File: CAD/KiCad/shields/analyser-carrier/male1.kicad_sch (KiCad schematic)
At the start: 5 parts, among them M4 DFRobot DFR0126 Audio Analyze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

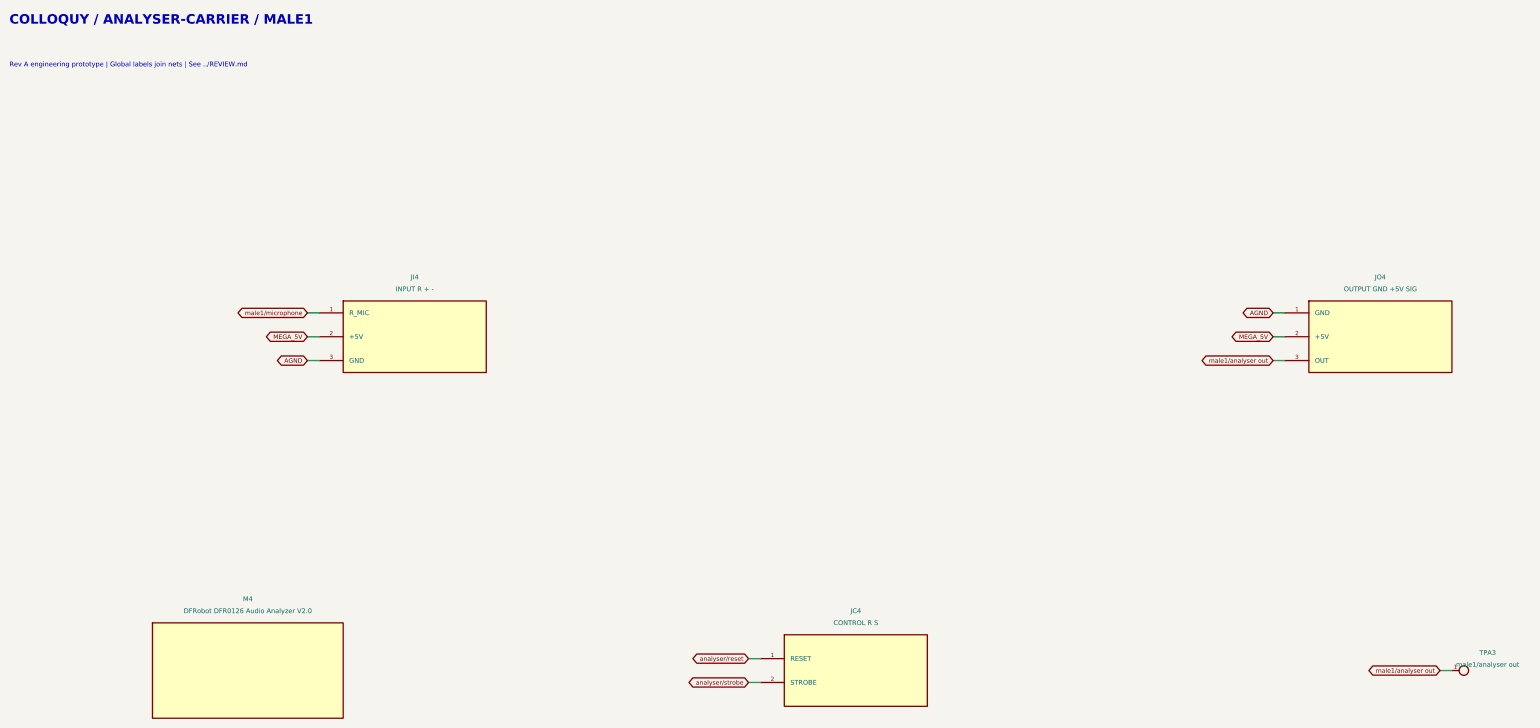
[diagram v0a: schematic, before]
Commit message: Convert analyser carrier to direct sockets for modified DFRobot modules
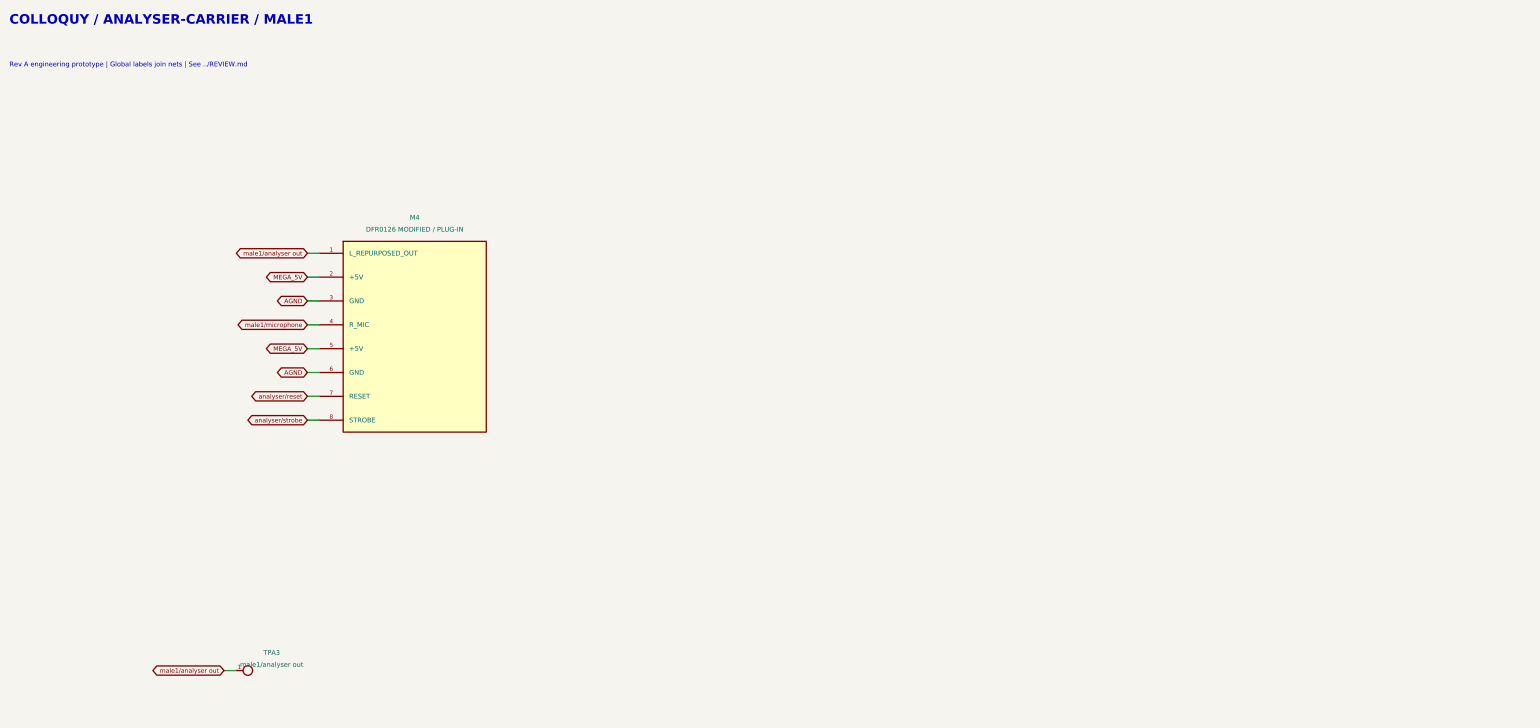
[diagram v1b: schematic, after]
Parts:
- removed JC4: CONTROL R S, Shields:PinHeader_1x02_P2.54mm_Vertical, symbol Colloquy:JC4
- removed JI4: INPUT R + -, Shields:PinHeader_1x03_P2.54mm_Vertical, symbol Colloquy:JI4
- removed JO4: OUTPUT GND +5V SIG, Shields:PinHeader_1x03_P2.54mm_Vertical, symbol Colloquy:JO4
- M4: value DFRobot DFR0126 Audio Analyzer V2.0 -> DFR0126 MODIFIED / PLUG-IN; footprint Shields:DFR0126_PhotoMount -> Shields:DFR0126_PlugIn_Photo
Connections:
- net AGND: now also M4.3 (GND), M4.6 (GND)
- net MEGA_5V: now also M4.2 (+5V), M4.5 (+5V)
- net analyser/reset: now also M4.7 (RESET)
- net analyser/strobe: now also M4.8 (STROBE)
- net male1/analyser out: now also M4.1 (L_REPURPOSED_OUT)
- net male1/microphone: now also M4.4 (R_MIC)
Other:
- moved on the sheet: TPA3

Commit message: Route the analyser carrier for microphones on the L inputs
Swap contacts 1 and 4 at all five DFRobot sites, regenerate schematics and route the carrier without moving pads or mounts. Update conversion labels, mechanical notes, both fabrication packages and actual-size fit templates.

Validation: native ERC/DRC/unconnected 0/0/0; independent pin/net and mating checks pass; 1796 pytest tests pass. Physical module fit remains unverified.
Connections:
- net male1/analyser out: now also M4.4 (R_REPURPOSED_OUT); no longer M4.1 (L_REPURPOSED_OUT)
- net male1/microphone: now also M4.1 (L_MIC); no longer M4.4 (R_MIC)
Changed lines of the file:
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@@
 (property "Footprint" "Shields:DFR0126_PlugIn_Photo" (at 101.6000 83.8200 0) (effects (font (size 1.27 1.27))  (hide yes)))
 (property "Datasheet" "https://wiki.dfrobot.com/dfr0126/" (at 101.6000 83.8200 0) (effects (font (size 1.27 1.27))  (hide yes)))
-(property "Description" "Modified module: remove module R4 (left-input 22K), jumper isolated L to OUT, fit downward 2.54mm headers. Carrier sockets: one 1x6 and one 1x2. Photo-derived geometry." (at 101.6000 83.8200 0) (effects (font (size 1.27 1.27))  (hide yes)))
+(property "Description" "Modified module: remove module R3 (right-input 22K), jumper isolated R to OUT, microphone on L, fit downward 2.54mm headers. Carrier sockets: one 1x6 and one 1x2. Photo-derived geometry." (at 101.6000 83.8200 0) (effects (font (size 1.27 1.27))  (hide yes)))
 (pin "1")
 (pin "2")
@@
 (instances (project "analyser-carrier" (path "/76417ac7-fbc7-56a8-ac79-79796e9479f5/9dc28e12-03c7-5a17-8b5a-98cb0f1f2dfa" (reference "M4") (unit 1)))))
 (wire (pts (xy 81.2800 66.0400) (xy 78.7400 66.0400)) (stroke (width 0) (type default)))
-(global_label "male1/analyser out" (shape bidirectional) (at 78.7400 66.0400 180) (effects (font (size 0.95 0.95)) (justify right)) (property "Intersheetrefs" "${INTERSHEET_REFS}" (at 78.7400 66.0400 0) (effects (font (size 1.016 1.016))  (hide yes))))
+(global_label "male1/microphone" (shape bidirectional) (at 78.7400 66.0400 180) (effects (font (size 0.95 0.95)) (justify right)) (property "Intersheetrefs" "${INTERSHEET_REFS}" (at 78.7400 66.0400 0) (effects (font (size 1.016 1.016))  (hide yes))))
 (wire (pts (xy 81.2800 71.1200) (xy 78.7400 71.1200)) (stroke (width 0) (type default)))
 (global_label "MEGA_5V" (shape bidirectional) (at 78.7400 71.1200 180) (effects (font (size 0.95 0.95)) (justify right)) (property "Intersheetrefs" "${INTERSHEET_REFS}" (at 78.7400 71.1200 0) (effects (font (size 1.016 1.016))  (hide yes))))
@@
 (global_label "AGND" (shape bidirectional) (at 78.7400 76.2000 180) (effects (font (size 0.95 0.95)) (justify right)) (property "Intersheetrefs" "${INTERSHEET_REFS}" (at 78.7400 76.2000 0) (effects (font (size 1.016 1.016))  (hide yes))))
 (wire (pts (xy 81.2800 81.2800) (xy 78.7400 81.2800)) (stroke (width 0) (type default)))
-(global_label "male1/microphone" (shape bidirectional) (at 78.7400 81.2800 180) (effects (font (size 0.95 0.95)) (justify right)) (property "Intersheetrefs" "${INTERSHEET_REFS}" (at 78.7400 81.2800 0) (effects (font (size 1.016 1.016))  (hide yes))))
+(global_label "male1/analyser out" (shape bidirectional) (at 78.7400 81.2800 180) (effects (font (size 0.95 0.95)) (justify right)) (property "Intersheetrefs" "${INTERSHEET_REFS}" (at 78.7400 81.2800 0) (effects (font (size 1.016 1.016))  (hide yes))))
 (wire (pts (xy 81.2800 86.3600) (xy 78.7400 86.3600)) (stroke (width 0) (type default)))
 (global_label "MEGA_5V" (shape bidirectional) (at 78.7400 86.3600 180) (effects (font (size 0.95 0.95)) (justify right)) (property "Intersheetrefs" "${INTERSHEET_REFS}" (at 78.7400 86.3600 0) (effects (font (size 1.016 1.016))  (hide yes))))
